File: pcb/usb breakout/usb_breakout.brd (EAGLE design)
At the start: 20 x 40 mm, 5 parts

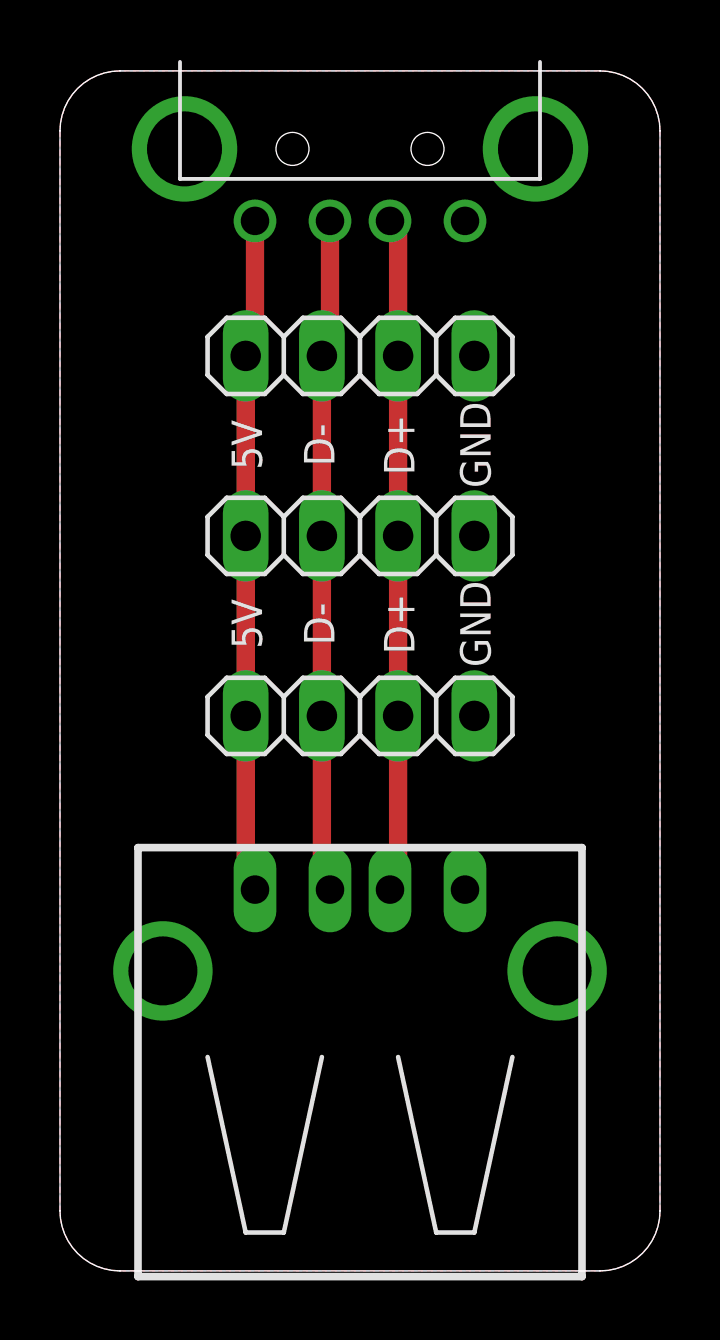
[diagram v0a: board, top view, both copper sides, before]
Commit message: updated usb breakout board
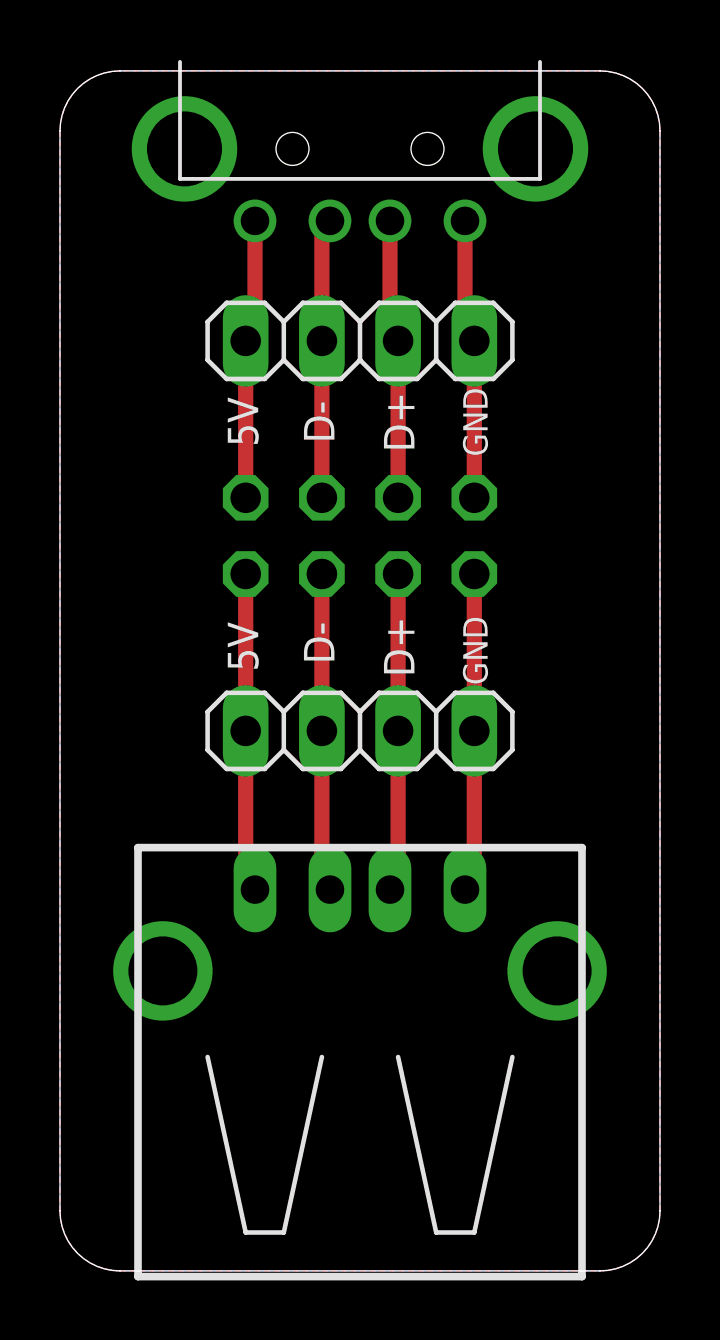
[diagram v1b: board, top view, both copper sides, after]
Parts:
- JP1: device pinhead:1X04 -> pinhead:2X04
- moved JP2 6.50 mm to (10.0, 31.0)
- moved JP1 6.00 mm to (10.0, 24.5), flipped to the bottom, turned to 180 degrees
- moved JP3 0.50 mm to (10.0, 18.0)
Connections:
- new net N$4: JP1.2, JP3.1, USB2.VBUS
- new net N$5: JP1.4, JP3.2, USB2.D-
- new net N$6: JP1.6, JP3.3, USB2.D+
- net GND: now also JP1.7, JP1.8, USB1.SHEELD2; no longer JP1.4
- net N$1: no longer JP3.1, USB2.VBUS
- net N$2: now also JP1.3; no longer JP1.2, JP3.2, USB2.D-
- net N$3: now also JP1.5; no longer JP1.3, JP3.3, USB2.D+
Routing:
- net GND: track 0.00 -> 20.0 mm
- net N$1: track 22.5 -> 9.36 mm
- net N$3: track 22.5 -> 9.34 mm
- net N$2: track 22.5 -> 9.34 mm
- net N$4: track 0.00 -> 10.6 mm
- net N$6: track 0.00 -> 10.6 mm
- net N$5: track 0.00 -> 10.6 mm
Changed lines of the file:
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@@
 <setting verticaltext="up"/>
 </settings>
-<grid distance="5" unitdist="mil" unit="mm" style="lines" multiple="1" display="no" altdistance="1" altunitdist="mil" altunit="mil"/>
+<grid distance="5" unitdist="mil" unit="mil" style="lines" multiple="1" display="no" altdistance="1" altunitdist="mil" altunit="mil"/>
 <layers>
 <layer number="1" name="Top" color="4" fill="1" visible="yes" active="yes"/>
@@
 <wire x1="0" y1="38" x2="0" y2="2" width="0" layer="20"/>
 <wire x1="0" y1="2" x2="2" y2="0" width="0" layer="20" curve="90"/>
-<text x="13.847" y="27.535" size="1.016" layer="25" rot="R90" align="center">GND</text>
-<text x="11.307" y="27.535" size="1.016" layer="25" rot="R90" align="center">D+</text>
-<text x="8.64" y="27.535" size="1.016" layer="25" rot="R90" align="center">D-</text>
-<text x="6.227" y="27.535" size="1.016" layer="25" rot="R90" align="center">5V</text>
-<text x="13.847" y="21.566" size="1.016" layer="25" rot="R90" align="center">GND</text>
-<text x="11.307" y="21.566" size="1.016" layer="25" rot="R90" align="center">D+</text>
-<text x="8.64" y="21.566" size="1.016" layer="25" rot="R90" align="center">D-</text>
-<text x="6.227" y="21.566" size="1.016" layer="25" rot="R90" align="center">5V</text>
+<text x="13.847" y="20.677" size="0.8128" layer="25" rot="R90" align="center">GND</text>
+<text x="11.307" y="28.297" size="1.016" layer="25" rot="R90" align="center">D+</text>
+<text x="8.64" y="28.297" size="1.016" layer="25" rot="R90" align="center">D-</text>
+<text x="6.1" y="20.804" size="1.016" layer="25" rot="R90" align="center">5V</text>
+<text x="11.307" y="20.804" size="1.016" layer="25" rot="R90" align="center">D+</text>
+<text x="8.64" y="20.931" size="1.016" layer="25" rot="R90" align="center">D-</text>
+<text x="6.1" y="28.297" size="1.016" layer="25" rot="R90" align="center">5V</text>
+<text x="13.847" y="28.297" size="0.8128" layer="25" rot="R90" align="center">GND</text>
 </plain>
 <attributes>
@@
 <attribute name="OC_NEWARK" value="unknown" x="10" y="10" size="1.778" layer="27" display="off"/>
 </element>
-<element name="JP1" library="pinhead" library_urn="urn:adsk.eagle:library:325" package="1X04" package3d_urn="urn:adsk.eagle:package:22407/2" value="" x="10" y="30.5" smashed="yes">
-<attribute name="POPULARITY" value="91" x="10" y="30.5" size="1.778" layer="27" display="off"/>
-<attribute name="VALUE" x="4.92" y="27.325" size="1.27" layer="27"/>
+<element name="JP1" library="pinhead" library_urn="urn:adsk.eagle:library:325" package="2X04" package3d_urn="urn:adsk.eagle:package:22461/2" value="" x="10" y="24.5" smashed="yes" rot="MR180">
+<attribute name="POPULARITY" value="47" x="10" y="24.5" size="1.778" layer="28" rot="MR180" display="off"/>
+<attribute name="VALUE" x="4.92" y="28.945" size="1.27" layer="28" rot="MR180"/>
 </element>
-<element name="JP2" library="pinhead" library_urn="urn:adsk.eagle:library:325" package="1X04" package3d_urn="urn:adsk.eagle:package:22407/2" value="" x="10" y="24.5" smashed="yes">
-<attribute name="POPULARITY" value="91" x="10" y="24.5" size="1.778" layer="27" display="off"/>
-<attribute name="VALUE" x="4.92" y="21.325" size="1.27" layer="27"/>
+<element name="JP2" library="pinhead" library_urn="urn:adsk.eagle:library:325" package="1X04" package3d_urn="urn:adsk.eagle:package:22407/2" value="" x="10" y="31" smashed="yes">
+<attribute name="POPULARITY" value="91" x="10" y="31" size="1.778" layer="27" display="off"/>
+<attribute name="VALUE" x="4.92" y="27.825" size="1.27" layer="27"/>
 </element>
-<element name="JP3" library="pinhead" library_urn="urn:adsk.eagle:library:325" package="1X04" package3d_urn="urn:adsk.eagle:package:22407/2" value="" x="10" y="18.5" smashed="yes">
-<attribute name="POPULARITY" value="91" x="10" y="18.5" size="1.778" layer="27" display="off"/>
-<attribute name="VALUE" x="4.92" y="15.325" size="1.27" layer="27"/>
+<element name="JP3" library="pinhead" library_urn="urn:adsk.eagle:library:325" package="1X04" package3d_urn="urn:adsk.eagle:package:22407/2" value="" x="10" y="18" smashed="yes">
+<attribute name="POPULARITY" value="91" x="10" y="18" size="1.778" layer="27" display="off"/>
+<attribute name="VALUE" x="4.92" y="14.825" size="1.27" layer="27"/>
 </element>
 </elements>
@@
 <contactref element="USB2" pad="S1"/>
 <contactref element="USB1" pad="GND"/>
-<contactref element="USB2" pad="GND"/>
-<contactref element="JP1" pad="4"/>
-<contactref element="JP2" pad="4"/>
-<contactref element="JP3" pad="4"/>
 <contactref element="USB1" pad="SHEELD"/>
 <polygon width="0.1524" layer="16" isolate="0.2794" rank="2">
@@
 <vertex x="0" y="38" curve="-90"/>
 </polygon>
+<contactref element="JP2" pad="4"/>
+<contactref element="JP1" pad="7"/>
+<contactref element="JP1" pad="8"/>
+<contactref element="JP3" pad="4"/>
+<contactref element="USB2" pad="GND"/>
+<wire x1="13.5" y1="35" x2="13.5" y2="31.31" width="0.508" layer="1"/>
+<wire x1="13.5" y1="31.31" x2="13.81" y2="31" width="0.508" layer="1"/>
+<wire x1="13.81" y1="31" x2="13.81" y2="25.77" width="0.508" layer="1"/>
+<wire x1="13.81" y1="23.23" x2="13.81" y2="18" width="0.508" layer="1"/>
+<wire x1="13.81" y1="18" x2="13.81" y2="13.02" width="0.508" layer="1"/>
+<wire x1="13.81" y1="13.02" x2="13.5" y2="12.71" width="0.508" layer="1"/>
+<contactref element="USB1" pad="SHEELD2"/>
 </signal>
 <signal name="N$1">
 <contactref element="USB1" pad="VBUS"/>
-<contactref element="USB2" pad="VBUS"/>
+<contactref element="JP2" pad="1"/>
 <contactref element="JP1" pad="1"/>
-<contactref element="JP2" pad="1"/>
-<contactref element="JP3" pad="1"/>
-<wire x1="6.5" y1="35" x2="6.5" y2="30.81" width="0.6096" layer="1"/>
-<wire x1="6.5" y1="30.81" x2="6.19" y2="30.5" width="0.6096" layer="1"/>
-<wire x1="6.19" y1="30.5" x2="6.19" y2="24.5" width="0.6096" layer="1"/>
-<wire x1="6.19" y1="24.5" x2="6.19" y2="18.5" width="0.6096" layer="1"/>
-<wire x1="6.19" y1="18.5" x2="6.19" y2="13.02" width="0.6096" layer="1"/>
-<wire x1="6.19" y1="13.02" x2="6.5" y2="12.71" width="0.6096" layer="1"/>
+<wire x1="6.5" y1="35" x2="6.5" y2="31.31" width="0.508" layer="1"/>
+<wire x1="6.5" y1="31.31" x2="6.19" y2="31" width="0.508" layer="1"/>
+<wire x1="6.19" y1="31" x2="6.19" y2="25.77" width="0.508" layer="1"/>
 </signal>
 <signal name="N$2">
 <contactref element="USB1" pad="D-"/>
-<contactref element="USB2" pad="D-"/>
-<contactref element="JP1" pad="2"/>
 <contactref element="JP2" pad="2"/>
-<contactref element="JP3" pad="2"/>
-<wire x1="9" y1="35" x2="9" y2="30.77" width="0.6096" layer="1"/>
-<wire x1="9" y1="30.77" x2="8.73" y2="30.5" width="0.6096" layer="1"/>
-<wire x1="8.73" y1="30.5" x2="8.73" y2="24.5" width="0.6096" layer="1"/>
-<wire x1="8.73" y1="24.5" x2="8.73" y2="18.5" width="0.6096" layer="1"/>
-<wire x1="8.73" y1="18.5" x2="8.73" y2="12.98" width="0.6096" layer="1"/>
-<wire x1="8.73" y1="12.98" x2="9" y2="12.71" width="0.6096" layer="1"/>
+<contactref element="JP1" pad="3"/>
+<wire x1="9" y1="35" x2="8.73" y2="34.73" width="0.508" layer="1"/>
+<wire x1="8.73" y1="34.73" x2="8.73" y2="31" width="0.508" layer="1"/>
+<wire x1="8.73" y1="31" x2="8.73" y2="25.77" width="0.508" layer="1"/>
 </signal>
 <signal name="N$3">
 <contactref element="USB1" pad="D+"/>
+<contactref element="JP2" pad="3"/>
+<contactref element="JP1" pad="5"/>
+<wire x1="11" y1="35" x2="11" y2="31.27" width="0.508" layer="1"/>
+<wire x1="11" y1="31.27" x2="11.27" y2="31" width="0.508" layer="1"/>
+<wire x1="11.27" y1="31" x2="11.27" y2="25.77" width="0.508" layer="1"/>
+</signal>
+<signal name="N$4">
+<contactref element="JP1" pad="2"/>
+<contactref element="JP3" pad="1"/>
+<contactref element="USB2" pad="VBUS"/>
+<wire x1="6.19" y1="23.23" x2="6.19" y2="18" width="0.508" layer="1"/>
+<wire x1="6.19" y1="18" x2="6.19" y2="13.02" width="0.508" layer="1"/>
+<wire x1="6.19" y1="13.02" x2="6.5" y2="12.71" width="0.508" layer="1"/>
+</signal>
+<signal name="N$5">
+<contactref element="JP1" pad="4"/>
+<contactref element="JP3" pad="2"/>
+<contactref element="USB2" pad="D-"/>
+<wire x1="8.73" y1="23.23" x2="8.73" y2="18" width="0.508" layer="1"/>
+<wire x1="8.73" y1="18" x2="8.73" y2="12.98" width="0.508" layer="1"/>
+<wire x1="8.73" y1="12.98" x2="9" y2="12.71" width="0.508" layer="1"/>
+</signal>
+<signal name="N$6">
+<contactref element="JP1" pad="6"/>
+<contactref element="JP3" pad="3"/>
 <contactref element="USB2" pad="D+"/>
-<contactref element="JP1" pad="3"/>
-<contactref element="JP2" pad="3"/>
-<contactref element="JP3" pad="3"/>
-<wire x1="11" y1="35" x2="11.27" y2="34.73" width="0.6096" layer="1"/>
-<wire x1="11.27" y1="34.73" x2="11.27" y2="30.5" width="0.6096" layer="1"/>
-<wire x1="11.27" y1="30.5" x2="11.27" y2="24.5" width="0.6096" layer="1"/>
-<wire x1="11.27" y1="24.5" x2="11.27" y2="18.5" width="0.6096" layer="1"/>
-<wire x1="11.27" y1="18.5" x2="11.27" y2="12.98" width="0.6096" layer="1"/>
-<wire x1="11.27" y1="12.98" x2="11" y2="12.71" width="0.6096" layer="1"/>
+<wire x1="11.27" y1="23.23" x2="11.27" y2="18" width="0.508" layer="1"/>
+<wire x1="11.27" y1="18" x2="11.27" y2="12.98" width="0.508" layer="1"/>
+<wire x1="11.27" y1="12.98" x2="11" y2="12.71" width="0.508" layer="1"/>
 </signal>
 </signals>
